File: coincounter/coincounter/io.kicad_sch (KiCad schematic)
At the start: 24 parts, among them J3 Conn_01x08, J4 Conn_01x02, Q10 Q_NPN_EBC, Q11 Q_NPN_EBC, Q7 Q_PNP_EBC, Q8 Q_NPN_EBC, Q9 Q_PNP_EBC, U4 L78L05_SOT89

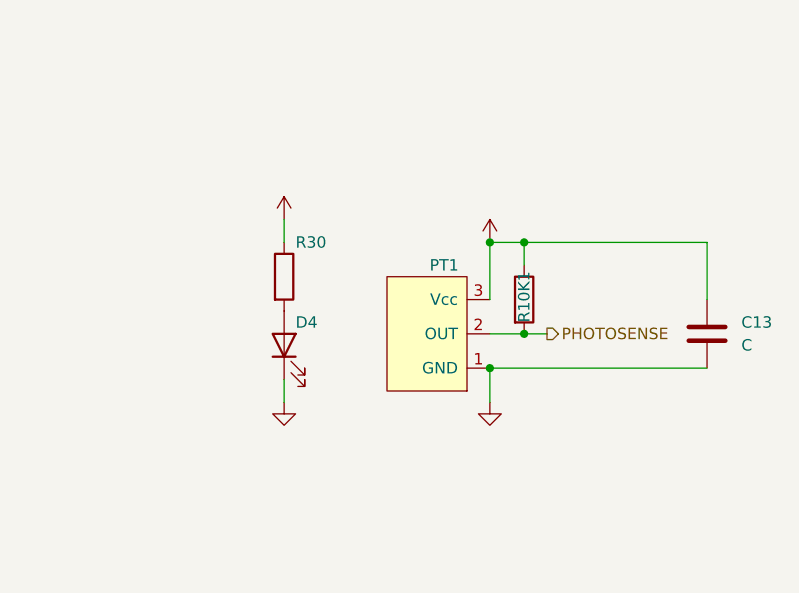
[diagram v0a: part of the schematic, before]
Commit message: Add flashing tool schematic, reorganize arduino files so the ide doesn't get confused, and improve ledstripesplitter so it even retimes the high pulses if the input is out of whack.
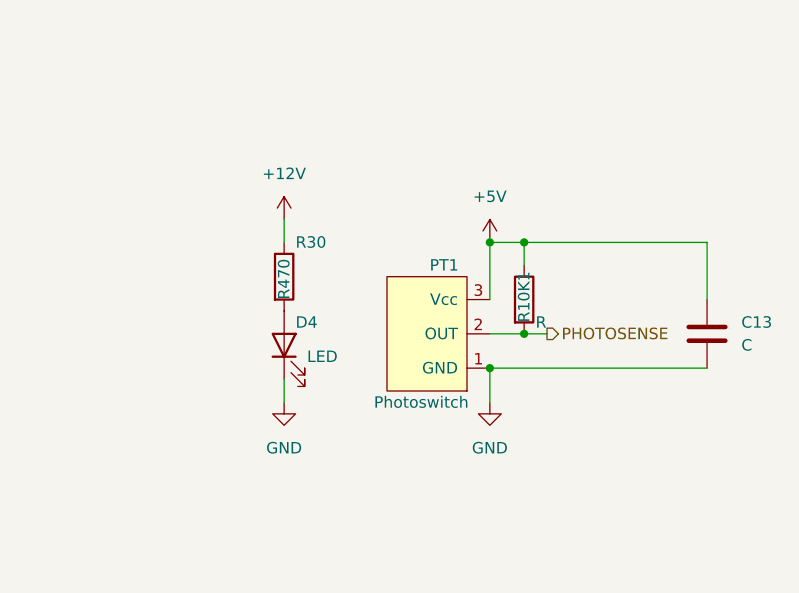
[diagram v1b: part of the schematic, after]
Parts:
- D4: value (none) -> LED
- PT1: value (none) -> Photoswitch
- R10K1: value (none) -> R
- R30: value (none) -> R470
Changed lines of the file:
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@@
       (effects (font (size 1.27 1.27)) hide)
     )
-    (property "Value" "" (id 1) (at 209.55 102.87 0))
+    (property "Value" "+5V" (id 1) (at 209.55 102.87 0))
     (property "Footprint" "" (id 2) (at 209.55 107.95 0)
       (effects (font (size 1.27 1.27)) hide)
@@
       (effects (font (size 1.27 1.27)) hide)
     )
-    (property "Value" "" (id 1) (at 209.55 130.81 0))
+    (property "Value" "GND" (id 1) (at 209.55 130.81 0))
     (property "Footprint" "" (id 2) (at 209.55 125.73 0)
       (effects (font (size 1.27 1.27)) hide)
@@
       (effects (font (size 1.27 1.27)) (justify left))
     )
-    (property "Value" "" (id 1) (at 186.69 114.3 90)
+    (property "Value" "R470" (id 1) (at 186.69 114.3 90)
       (effects (font (size 1.27 1.27)) (justify left))
     )
@@
     (in_bom yes) (on_board yes)
     (property "Reference" "PT1" (id 0) (at 204.47 110.49 0))
-    (property "Value" "" (id 1) (at 201.93 125.73 0))
+    (property "Value" "Photoswitch" (id 1) (at 201.93 125.73 0))
     (property "Footprint" "" (id 2) (at 199.39 118.11 0)
       (effects (font (size 1.27 1.27)) hide)
@@
       (effects (font (size 1.27 1.27)) hide)
     )
-    (property "Value" "" (id 1) (at 186.69 100.33 0))
+    (property "Value" "+12V" (id 1) (at 186.69 100.33 0))
     (property "Footprint" "" (id 2) (at 186.69 105.41 0)
       (effects (font (size 1.27 1.27)) hide)
@@
       (effects (font (size 1.27 1.27)) (justify left))
     )
-    (property "Value" "" (id 1) (at 214.63 116.84 0)
+    (property "Value" "R" (id 1) (at 214.63 116.84 0)
       (effects (font (size 1.27 1.27)) (justify left))
     )
@@
       (effects (font (size 1.27 1.27)) hide)
     )
-    (property "Value" "" (id 1) (at 186.69 130.81 0))
+    (property "Value" "GND" (id 1) (at 186.69 130.81 0))
     (property "Footprint" "" (id 2) (at 186.69 125.73 0)
       (effects (font (size 1.27 1.27)) hide)
@@
       (effects (font (size 1.27 1.27)) (justify right))
     )
-    (property "Value" "" (id 1) (at 189.23 120.65 90)
+    (property "Value" "LED" (id 1) (at 189.23 120.65 90)
       (effects (font (size 1.27 1.27)) (justify right))
     )
